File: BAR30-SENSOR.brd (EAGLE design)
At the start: 11.5 x 11.5 mm, 16 parts, among them Q1 BSS138, Q2 BSS138

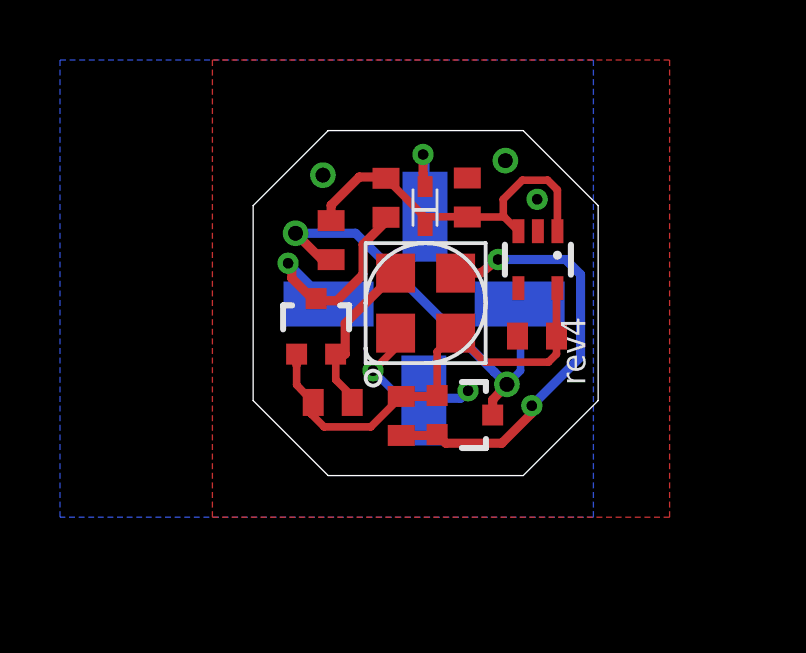
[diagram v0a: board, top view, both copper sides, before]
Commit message: Last minute major redesign for DroneCode I2C compatibility.
PixHawk and others cannot handle 5V I2C logic but have 5V I2C power supplies!
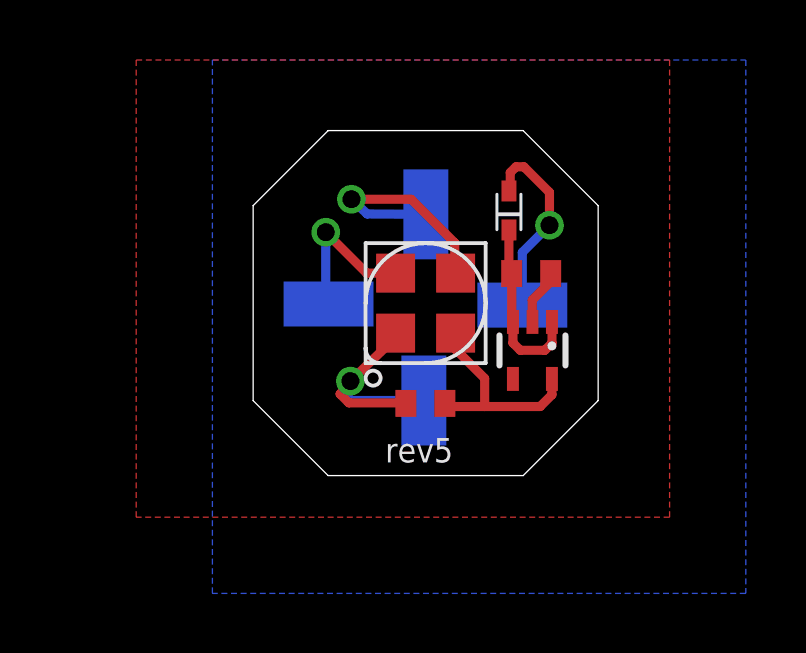
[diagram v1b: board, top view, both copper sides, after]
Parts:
- removed Q1, Q2: BSS138, SparkFun-DiscreteSemi:SOT323
- removed R2, R3, R4, R5: 10K, resistor:R0402
- moved U$4 4.38 mm to (10.3, 7.07), turned to 180 degrees
- moved C1 4.35 mm to (7.10, 3.79)
- moved U$5 4.33 mm to (7.11, 10.1), turned to 270 degrees
- moved C2 3.31 mm to (10.6, 8.12), turned to 0 degrees
- moved U$8 3.03 mm to (10.7, 5.56)
- moved D1 2.80 mm to (9.88, 10.2)
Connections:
- removed net SCL_HV: Q2.3, R5.1, U$5.P$1
- removed net SCL_LV: Q2.2, R4.1, U$1.3
- removed net SDA_HV: Q1.3, R3.1, U$6.P$1
- removed net SDA_LV: Q1.2, R2.1, U$1.4
- new net SCL: U$1.3, U$5.P$1
- new net SDA: U$1.4, U$6.P$1
- net 3.3V: no longer Q1.1, Q2.1, R2.2, R4.2
- net VCC: no longer R3.2, R5.2
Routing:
- net SCL_HV: track 14.8 -> 0.00 mm, vias 2 -> 0
- net SCL_LV: track 14.7 -> 0.00 mm, vias 2 -> 0
- net 3.3V: track 15.4 -> 7.15 mm
- net SDA_HV: track 7.81 -> 0.00 mm, vias 1 -> 0
- net SCL: track 0.00 -> 7.74 mm, vias 0 -> 1
- net VCC: track 12.4 -> 6.03 mm
- net SDA_LV: track 5.54 -> 0.00 mm
- net SDA: track 0.00 -> 5.33 mm, vias 0 -> 1
- net GND: track 5.28 -> 10.2 mm, vias 5 -> 1
- net VIN: track 3.30 -> 6.51 mm
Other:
- board text added: "rev5"
- board text removed: "rev4"
